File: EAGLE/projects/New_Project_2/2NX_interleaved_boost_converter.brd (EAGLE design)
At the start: 143.5 x 151.1 mm, 36 parts, among them J1 26-60-4050, J3 66.9040-22, J4 66.9040-22, J5 66.9040-22, J6 66.9040-22, J7 26-60-4050, Q1 C2M0160120D, Q2 C2M0160120D

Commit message: some corrections in eagle
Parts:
- moved J7 16.7 mm to (43.8, 66.7), turned to 180 degrees
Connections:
- net GND: now also J7.5, Q2.3; no longer J7.1, Q2.2
- net N$5: now also J7.1, Q2.2; no longer J7.5, Q2.3
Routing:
- net GND: track 110.6 -> 46.0 mm
- net N$5: track 26.9 -> 70.8 mm
- net N$13: track 16.5 -> 19.2 mm
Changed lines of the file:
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@@
 <attribute name="VALUE" x="67.31" y="60.96" size="1.27" layer="27" rot="R270" align="center"/>
 </element>
-<element name="J7" library="SamacSys_Parts" package="SHDR5W155P0X396_1X5_1966X1001X" value="26-60-4050" x="60.325" y="69.215" smashed="yes">
-<attribute name="DESCRIPTION" value="Molex KK 396 Series, Series Number 41791, 3.96mm Pitch 5 Way 1 Row Straight PCB Header, Solder Termination, 7A" x="60.325" y="69.215" size="1.778" layer="27" display="off"/>
-<attribute name="HEIGHT" value="14.78mm" x="60.325" y="69.215" size="1.778" layer="27" display="off"/>
-<attribute name="MANUFACTURER_NAME" value="Molex" x="60.325" y="69.215" size="1.778" layer="27" display="off"/>
-<attribute name="MANUFACTURER_PART_NUMBER" value="26-60-4050" x="60.325" y="69.215" size="1.778" layer="27" display="off"/>
-<attribute name="MOUSER_PART_NUMBER" value="538-26-60-4050" x="60.325" y="69.215" size="1.778" layer="27" display="off"/>
-<attribute name="NAME" x="46.355" y="65.405" size="1.27" layer="25" align="center"/>
-<attribute name="VALUE" x="52.705" y="65.405" size="1.27" layer="27" align="center"/>
+<element name="J7" library="SamacSys_Parts" package="SHDR5W155P0X396_1X5_1966X1001X" value="26-60-4050" x="43.815" y="66.675" smashed="yes" rot="R180">
+<attribute name="DESCRIPTION" value="Molex KK 396 Series, Series Number 41791, 3.96mm Pitch 5 Way 1 Row Straight PCB Header, Solder Termination, 7A" x="43.815" y="66.675" size="1.778" layer="27" rot="R180" display="off"/>
+<attribute name="HEIGHT" value="14.78mm" x="43.815" y="66.675" size="1.778" layer="27" rot="R180" display="off"/>
+<attribute name="MANUFACTURER_NAME" value="Molex" x="43.815" y="66.675" size="1.778" layer="27" rot="R180" display="off"/>
+<attribute name="MANUFACTURER_PART_NUMBER" value="26-60-4050" x="43.815" y="66.675" size="1.778" layer="27" rot="R180" display="off"/>
+<attribute name="MOUSER_PART_NUMBER" value="538-26-60-4050" x="43.815" y="66.675" size="1.778" layer="27" rot="R180" display="off"/>
+<attribute name="NAME" x="57.785" y="70.485" size="1.27" layer="25" rot="R180" align="center"/>
+<attribute name="VALUE" x="51.435" y="70.485" size="1.27" layer="27" rot="R180" align="center"/>
 </element>
 <element name="U$1" library="heatsink" library_urn="urn:adsk.eagle:library:236" package="FK213" package3d_urn="urn:adsk.eagle:package:14197/1" value="" x="107.95" y="138.43" smashed="yes">
@@
 <contactref element="J6" pad="3"/>
 <contactref element="J6" pad="4"/>
-<contactref element="Q2" pad="2"/>
 <contactref element="Q1" pad="3"/>
 <contactref element="C3" pad="1"/>
 <contactref element="D4" pad="1"/>
 <contactref element="C5" pad="2"/>
-<contactref element="J7" pad="1"/>
 <contactref element="J1" pad="5"/>
 <polygon width="2.54" layer="16" thermals="no">
@@
 <wire x1="43.85" y1="75.53" x2="44.45" y2="74.93" width="5.08" layer="16"/>
 <wire x1="44.45" y1="74.93" x2="44.45" y2="76.2" width="5.08" layer="16"/>
-<wire x1="60.325" y1="69.215" x2="60.325" y2="73.025" width="5.08" layer="16"/>
-<wire x1="60.325" y1="73.025" x2="60.96" y2="73.66" width="5.08" layer="16"/>
 <wire x1="66.04" y1="85.005" x2="66.04" y2="78.74" width="5.08" layer="16"/>
 <wire x1="108.75" y1="61.87" x2="110.93" y2="59.69" width="3.048" layer="16"/>
-<wire x1="66.04" y1="61.87" x2="108.75" y2="61.87" width="3.048" layer="16"/>
-<wire x1="66.04" y1="61.87" x2="67.67" y2="63.5" width="3.048" layer="16"/>
-<wire x1="67.67" y1="63.5" x2="74.93" y2="63.5" width="3.048" layer="16"/>
-<wire x1="74.93" y1="63.5" x2="73.3" y2="61.87" width="3.048" layer="16"/>
-<wire x1="73.3" y1="61.87" x2="66.04" y2="61.87" width="3.048" layer="16"/>
-<wire x1="66.04" y1="61.87" x2="71.48" y2="67.31" width="3.048" layer="16"/>
-<wire x1="71.48" y1="67.31" x2="74.93" y2="67.31" width="3.048" layer="16"/>
-<wire x1="74.93" y1="67.31" x2="72.39" y2="64.77" width="3.048" layer="16"/>
-<wire x1="66.04" y1="61.87" x2="69.85" y2="65.68" width="3.048" layer="16"/>
-<wire x1="69.85" y1="65.68" x2="69.85" y2="69.85" width="3.048" layer="16"/>
+<contactref element="J7" pad="5"/>
+<contactref element="Q2" pad="3"/>
+<wire x1="59.655" y1="66.675" x2="59.655" y2="74.895" width="3.81" layer="16"/>
+<wire x1="59.655" y1="74.895" x2="59.69" y2="74.93" width="3.81" layer="16"/>
+<wire x1="66.04" y1="56.43" x2="70.4" y2="56.43" width="5.08" layer="16"/>
+<wire x1="70.4" y1="56.43" x2="80.01" y2="66.04" width="5.08" layer="16"/>
 </signal>
 <signal name="VCC">
@@
 <signal name="N$5">
 <contactref element="L2" pad="2"/>
-<contactref element="Q2" pad="3"/>
 <contactref element="C2" pad="2"/>
-<contactref element="J7" pad="5"/>
-<wire x1="44.485" y1="69.215" x2="57.27" y2="56.43" width="2.54" layer="1"/>
-<wire x1="57.27" y1="56.43" x2="66.04" y2="56.43" width="2.54" layer="1"/>
-<polygon width="2.54" layer="16" thermals="no">
-<vertex x="64.77" y="58.42"/>
-<vertex x="67.31" y="58.42"/>
-<vertex x="68.58" y="57.15"/>
+<contactref element="J7" pad="1"/>
+<contactref element="Q2" pad="2"/>
+<wire x1="43.815" y1="66.675" x2="50.8" y2="59.69" width="2.54" layer="1"/>
+<wire x1="50.8" y1="59.69" x2="52.07" y2="58.42" width="2.54" layer="1"/>
+<wire x1="62.59" y1="58.42" x2="66.04" y2="61.87" width="2.54" layer="1"/>
+<wire x1="52.07" y1="58.42" x2="62.59" y2="58.42" width="2.54" layer="1"/>
+<wire x1="55.68" y1="30.48" x2="55.68" y2="33.65" width="5.08" layer="16"/>
+<wire x1="55.68" y1="33.65" x2="67.31" y2="45.28" width="5.08" layer="16"/>
+<wire x1="66.04" y1="61.87" x2="63.14" y2="61.87" width="5.08" layer="16"/>
+<wire x1="63.14" y1="61.87" x2="59.69" y2="58.42" width="5.08" layer="16"/>
+<wire x1="59.69" y1="58.42" x2="59.69" y2="52.9" width="5.08" layer="16"/>
+<wire x1="59.69" y1="52.9" x2="67.31" y2="45.28" width="5.08" layer="16"/>
+<wire x1="50.8" y1="59.69" x2="50.8" y2="59.69" width="2.54" layer="1"/>
+<polygon width="2.54" layer="16" thermals="no">
+<vertex x="52.07" y="31.75"/>
+<vertex x="52.07" y="29.21"/>
+<vertex x="54.61" y="26.67"/>
+<vertex x="57.15" y="26.67"/>
+<vertex x="59.69" y="29.21"/>
+<vertex x="59.69" y="31.75"/>
+<vertex x="57.15" y="34.29"/>
+<vertex x="54.61" y="34.29"/>
+</polygon>
+<polygon width="2.54" layer="16" thermals="no">
+<vertex x="66.04" y="48.26"/>
+<vertex x="68.58" y="48.26"/>
+<vertex x="69.85" y="46.99"/>
+<vertex x="69.85" y="44.45"/>
 <vertex x="68.58" y="43.18"/>
-<vertex x="60.96" y="35.56"/>
-<vertex x="58.42" y="33.02"/>
-<vertex x="58.42" y="29.21"/>
-<vertex x="57.15" y="27.94"/>
-<vertex x="54.61" y="27.94"/>
-<vertex x="53.34" y="29.21"/>
-<vertex x="53.34" y="31.75"/>
-<vertex x="66.04" y="44.45"/>
-<vertex x="66.04" y="53.34"/>
-<vertex x="64.77" y="54.61"/>
-<vertex x="63.5" y="55.88"/>
-<vertex x="63.5" y="57.15"/>
+<vertex x="66.04" y="43.18"/>
+<vertex x="64.77" y="44.45"/>
+<vertex x="64.77" y="46.99"/>
 </polygon>
 </signal>
@@
 </polygon>
 </signal>
-<signal name="N$11">
-<contactref element="J7" pad="3"/>
-<contactref element="Q2" pad="1"/>
-<wire x1="66.04" y1="67.31" x2="63.5" y2="64.77" width="2.54" layer="1"/>
-<wire x1="56.85" y1="64.77" x2="52.405" y2="69.215" width="2.54" layer="1"/>
-<wire x1="63.5" y1="64.77" x2="56.85" y2="64.77" width="2.54" layer="1"/>
-</signal>
 <signal name="N$12">
 <contactref element="J1" pad="3"/>
@@
 <wire x1="63.835" y1="95.885" x2="66.04" y2="95.885" width="2.54" layer="1"/>
 </signal>
+<signal name="N$13">
+<contactref element="J7" pad="3"/>
+<contactref element="Q2" pad="1"/>
+<wire x1="66.04" y1="67.31" x2="60.96" y2="62.23" width="2.54" layer="1"/>
+<wire x1="51.735" y1="65.105" x2="51.735" y2="66.675" width="2.54" layer="1"/>
+<wire x1="60.96" y1="62.23" x2="54.61" y2="62.23" width="2.54" layer="1"/>
+<wire x1="54.61" y1="62.23" x2="51.735" y2="65.105" width="2.54" layer="1"/>
+</signal>
 </signals>

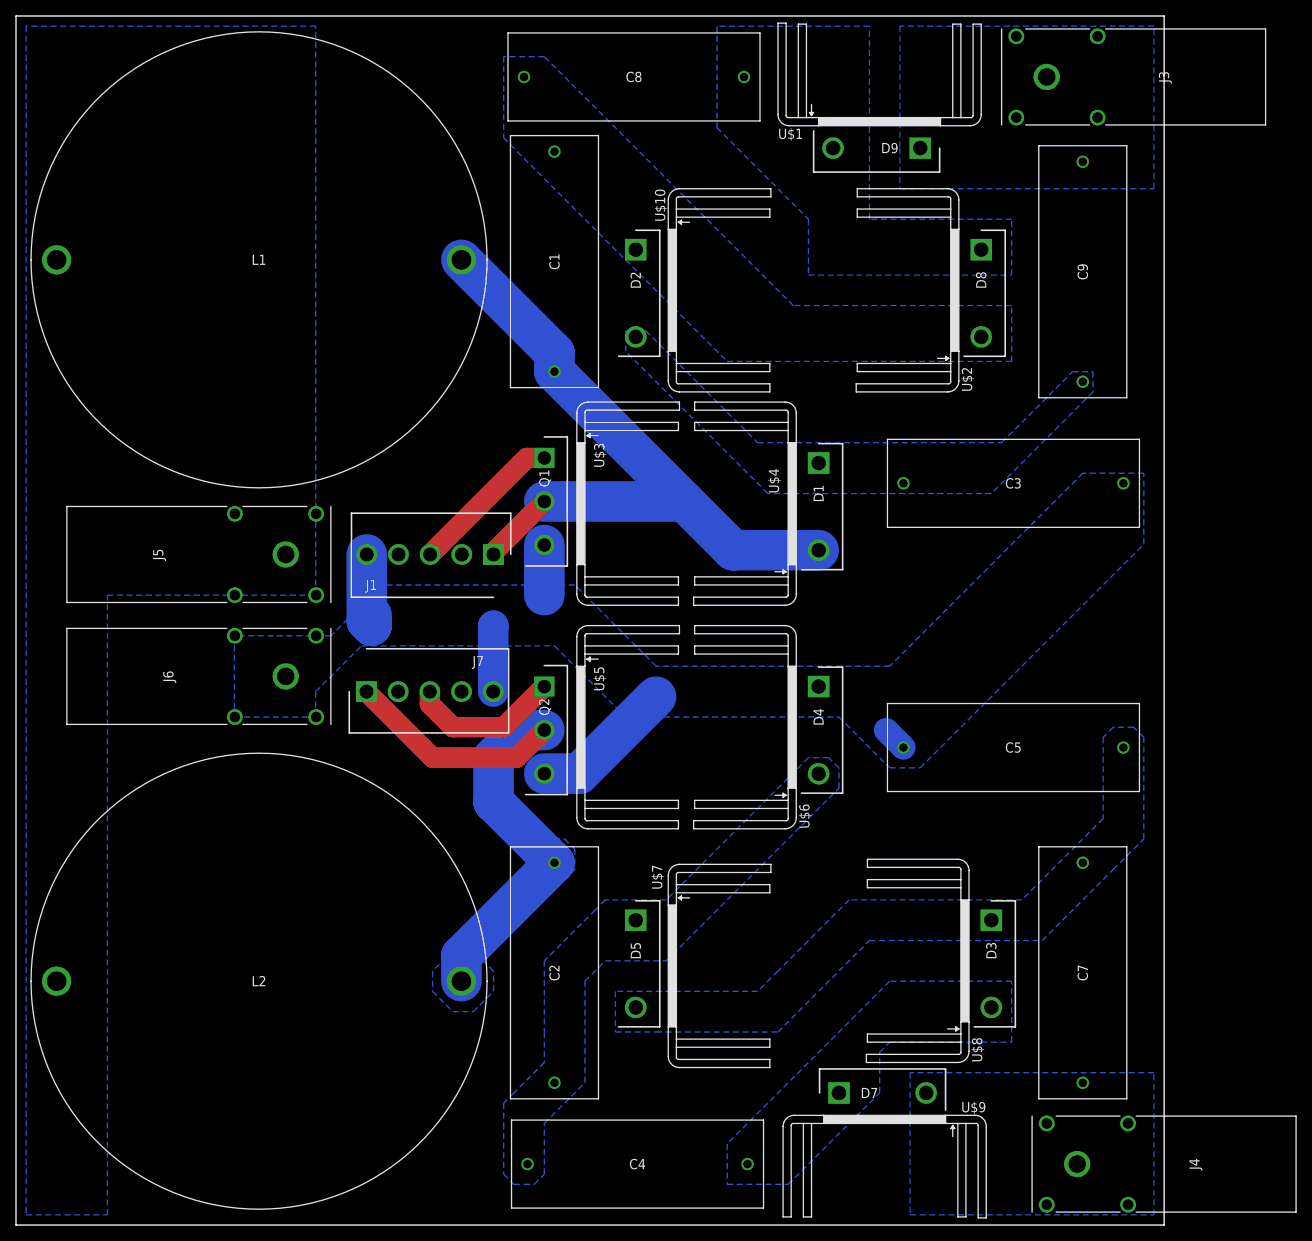
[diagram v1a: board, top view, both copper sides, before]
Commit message: wrote about pcb design
only about my own work, not about good collaboration with sugar
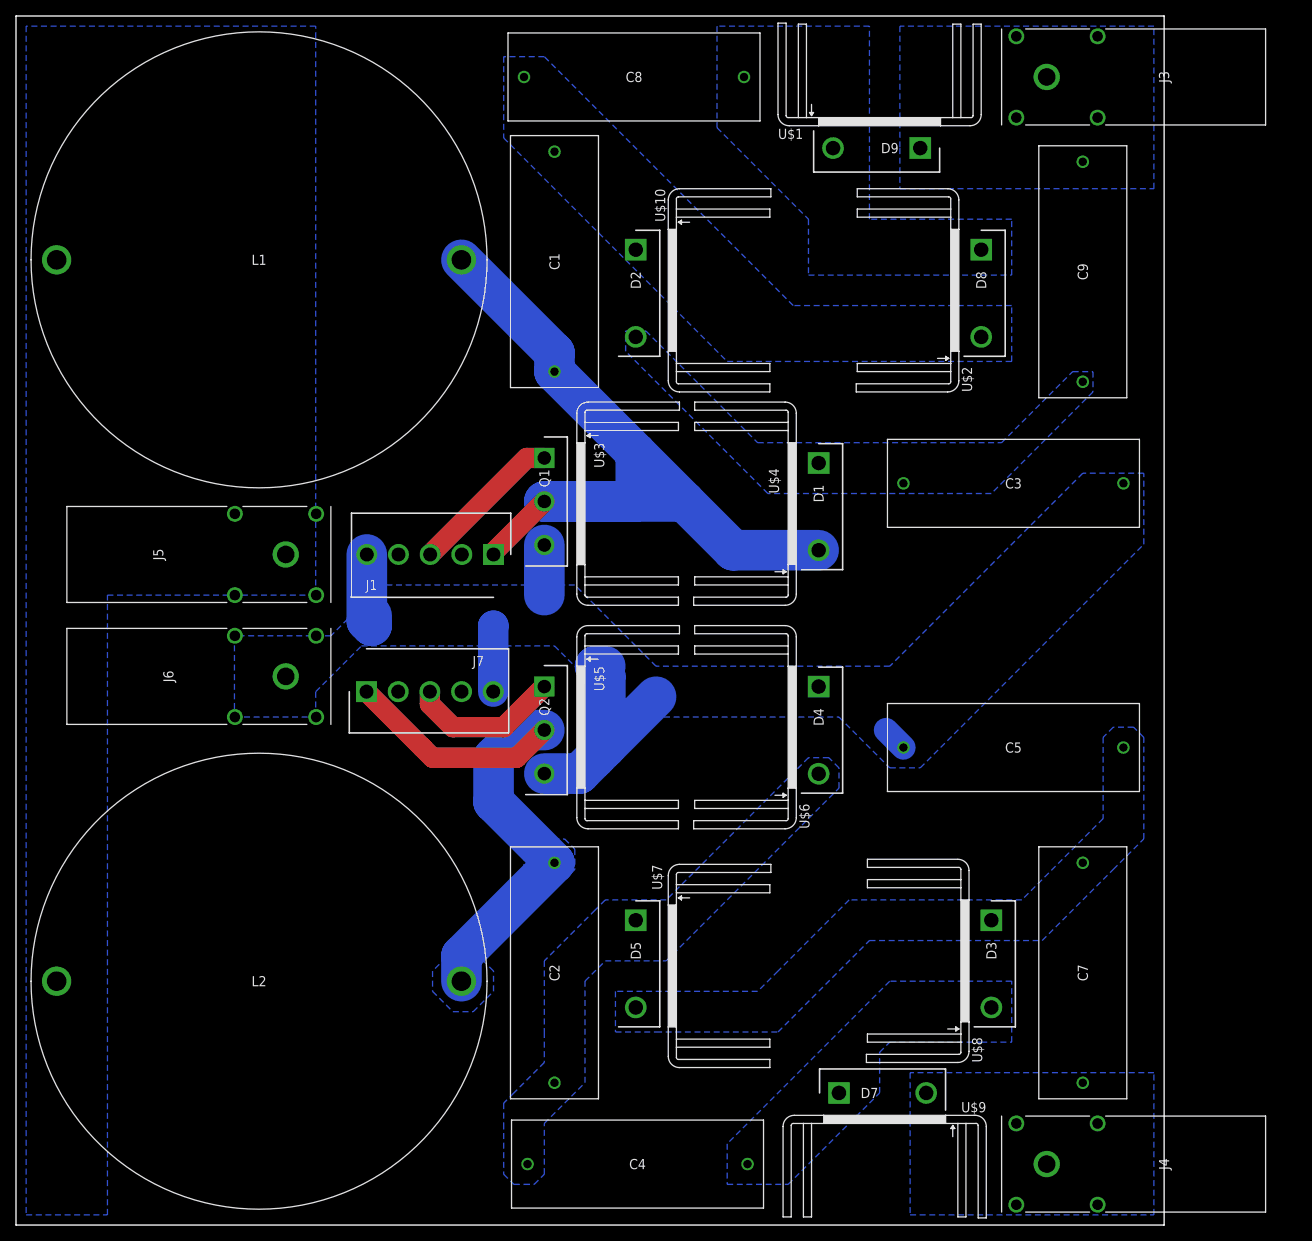
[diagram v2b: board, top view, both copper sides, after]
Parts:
- moved J4 3.81 mm to (139.7, 7.62)
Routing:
- net N$2: track 87.8 -> 105.3 mm
- net GND: track 46.0 -> 57.9 mm
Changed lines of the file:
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@@
 <wire x1="143.5154" y1="151.1302" x2="0" y2="151.1302" width="0" layer="20"/>
 <wire x1="0" y1="151.1302" x2="0" y2="0" width="0" layer="20"/>
+<dimension x1="0" y1="151.1302" x2="143.51" y2="151.13" x3="71.75500625" y3="153.67004375" textsize="1.778" layer="20"/>
+<dimension x1="143.5154" y1="151.1302" x2="143.51" y2="0" x3="146.051928125" y3="75.565009375" textsize="1.778" layer="20"/>
 </plain>
 <attributes>
@@
 <attribute name="VALUE" x="142.24" y="143.51" size="1.27" layer="27" rot="R270" align="center"/>
 </element>
-<element name="J4" library="SamacSys_Parts" package="66904022" value="66.9040-22" x="143.51" y="7.62" smashed="yes" rot="R270">
-<attribute name="ALLIED_NUMBER" value="70749834" x="64.77" y="-27.94" size="1.778" layer="27" rot="R270" display="off"/>
-<attribute name="ALLIED_PRICE-STOCK" value="https://www.alliedelec.com/staubli-66-9040-22/70749834/" x="64.77" y="-27.94" size="1.778" layer="27" rot="R270" display="off"/>
-<attribute name="ARROW_PART_NUMBER" value="66.9040-22" x="64.77" y="-27.94" size="1.778" layer="27" rot="R270" display="off"/>
-<attribute name="ARROW_PRICE-STOCK" value="" x="64.77" y="-27.94" size="1.778" layer="27" rot="R270" display="off"/>
-<attribute name="DESCRIPTION" value="STAUBLI - 66.9040-22 - SOCKET, PCB, 4MM, R/A, RED" x="64.77" y="-27.94" size="1.778" layer="27" rot="R270" display="off"/>
-<attribute name="HEIGHT" value="11mm" x="64.77" y="-27.94" size="1.778" layer="27" rot="R270" display="off"/>
-<attribute name="MANUFACTURER_NAME" value="STAUBLI" x="64.77" y="-27.94" size="1.778" layer="27" rot="R270" display="off"/>
-<attribute name="MANUFACTURER_PART_NUMBER" value="66.9040-22" x="64.77" y="-27.94" size="1.778" layer="27" rot="R270" display="off"/>
-<attribute name="NAME" x="147.32" y="7.62" size="1.27" layer="25" rot="R270" align="center"/>
-<attribute name="RS_PART_NUMBER" value="" x="64.77" y="-27.94" size="1.778" layer="27" rot="R270" display="off"/>
-<attribute name="RS_PRICE-STOCK" value="" x="64.77" y="-27.94" size="1.778" layer="27" rot="R270" display="off"/>
-<attribute name="VALUE" x="146.05" y="7.62" size="1.27" layer="27" rot="R270" align="center"/>
+<element name="J4" library="SamacSys_Parts" package="66904022" value="66.9040-22" x="139.7" y="7.62" smashed="yes" rot="R270">
+<attribute name="ALLIED_NUMBER" value="70749834" x="60.96" y="-27.94" size="1.778" layer="27" rot="R270" display="off"/>
+<attribute name="ALLIED_PRICE-STOCK" value="https://www.alliedelec.com/staubli-66-9040-22/70749834/" x="60.96" y="-27.94" size="1.778" layer="27" rot="R270" display="off"/>
+<attribute name="ARROW_PART_NUMBER" value="66.9040-22" x="60.96" y="-27.94" size="1.778" layer="27" rot="R270" display="off"/>
+<attribute name="ARROW_PRICE-STOCK" value="" x="60.96" y="-27.94" size="1.778" layer="27" rot="R270" display="off"/>
+<attribute name="DESCRIPTION" value="STAUBLI - 66.9040-22 - SOCKET, PCB, 4MM, R/A, RED" x="60.96" y="-27.94" size="1.778" layer="27" rot="R270" display="off"/>
+<attribute name="HEIGHT" value="11mm" x="60.96" y="-27.94" size="1.778" layer="27" rot="R270" display="off"/>
+<attribute name="MANUFACTURER_NAME" value="STAUBLI" x="60.96" y="-27.94" size="1.778" layer="27" rot="R270" display="off"/>
+<attribute name="MANUFACTURER_PART_NUMBER" value="66.9040-22" x="60.96" y="-27.94" size="1.778" layer="27" rot="R270" display="off"/>
+<attribute name="NAME" x="143.51" y="7.62" size="1.27" layer="25" rot="R270" align="center"/>
+<attribute name="RS_PART_NUMBER" value="" x="60.96" y="-27.94" size="1.778" layer="27" rot="R270" display="off"/>
+<attribute name="RS_PRICE-STOCK" value="" x="60.96" y="-27.94" size="1.778" layer="27" rot="R270" display="off"/>
+<attribute name="VALUE" x="142.24" y="7.62" size="1.27" layer="27" rot="R270" align="center"/>
 </element>
 <element name="J5" library="SamacSys_Parts" package="66904022" value="66.9040-22" x="22.86" y="83.82" smashed="yes" rot="R90">
@@
 <wire x1="59.655" y1="74.895" x2="59.69" y2="74.93" width="3.81" layer="16"/>
 <wire x1="66.04" y1="56.43" x2="70.4" y2="56.43" width="5.08" layer="16"/>
-<wire x1="70.4" y1="56.43" x2="80.01" y2="66.04" width="5.08" layer="16"/>
+<wire x1="70.4" y1="56.43" x2="72.39" y2="58.42" width="5.08" layer="16"/>
+<wire x1="73.66" y1="59.69" x2="80.01" y2="66.04" width="5.08" layer="16"/>
+<wire x1="72.39" y1="58.42" x2="73.66" y2="59.69" width="5.08" layer="16"/>
+<wire x1="73.66" y1="59.69" x2="73.66" y2="68.58" width="5.08" layer="16"/>
+<wire x1="73.66" y1="68.58" x2="72.39" y2="69.85" width="5.08" layer="16"/>
+<wire x1="72.39" y1="69.85" x2="73.66" y2="69.85" width="5.08" layer="16"/>
 </signal>
 <signal name="VCC">
@@
 <wire x1="55.68" y1="120.65" x2="67.31" y2="109.02" width="5.08" layer="16"/>
 <wire x1="67.31" y1="109.02" x2="67.31" y2="106.68" width="5.08" layer="16"/>
-<wire x1="67.31" y1="106.68" x2="83.545" y2="90.445" width="5.08" layer="16"/>
+<wire x1="67.31" y1="106.68" x2="77.47" y2="96.52" width="5.08" layer="16"/>
+<wire x1="77.47" y1="96.52" x2="83.545" y2="90.445" width="5.08" layer="16"/>
 <wire x1="89.64" y1="84.35" x2="100.33" y2="84.35" width="5.08" layer="16"/>
+<wire x1="83.545" y1="90.445" x2="89.64" y2="84.35" width="5.08" layer="16"/>
 <wire x1="66.04" y1="90.445" x2="83.545" y2="90.445" width="5.08" layer="16"/>
-<wire x1="83.545" y1="90.445" x2="89.64" y2="84.35" width="5.08" layer="16"/>
+<wire x1="66.04" y1="90.445" x2="77.47" y2="90.445" width="5.08" layer="16"/>
+<wire x1="77.47" y1="90.445" x2="77.47" y2="96.52" width="5.08" layer="16"/>
 </signal>
 <signal name="N$8">
@@
 </polygon>
 <polygon width="2.54" layer="16" thermals="no">
-<vertex x="66.04" y="48.26"/>
+<vertex x="64.77" y="48.26"/>
 <vertex x="68.58" y="48.26"/>
 <vertex x="69.85" y="46.99"/>
 <vertex x="69.85" y="44.45"/>
 <vertex x="68.58" y="43.18"/>
-<vertex x="66.04" y="43.18"/>
-<vertex x="64.77" y="44.45"/>
-<vertex x="64.77" y="46.99"/>
+<vertex x="63.5" y="43.18"/>
+<vertex x="63.5" y="46.99"/>
 </polygon>
 </signal>
